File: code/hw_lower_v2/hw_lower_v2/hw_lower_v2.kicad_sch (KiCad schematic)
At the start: 22 parts, among them J1 Screw_Terminal_01x01, J2 Screw_Terminal_01x01, J3 Screw_Terminal_01x01, J4 Screw_Terminal_01x01, J5 Screw_Terminal_01x01, J6 Screw_Terminal_01x01, J7 Conn_01x06_Pin, J8 Conn_02x20_Odd_Even

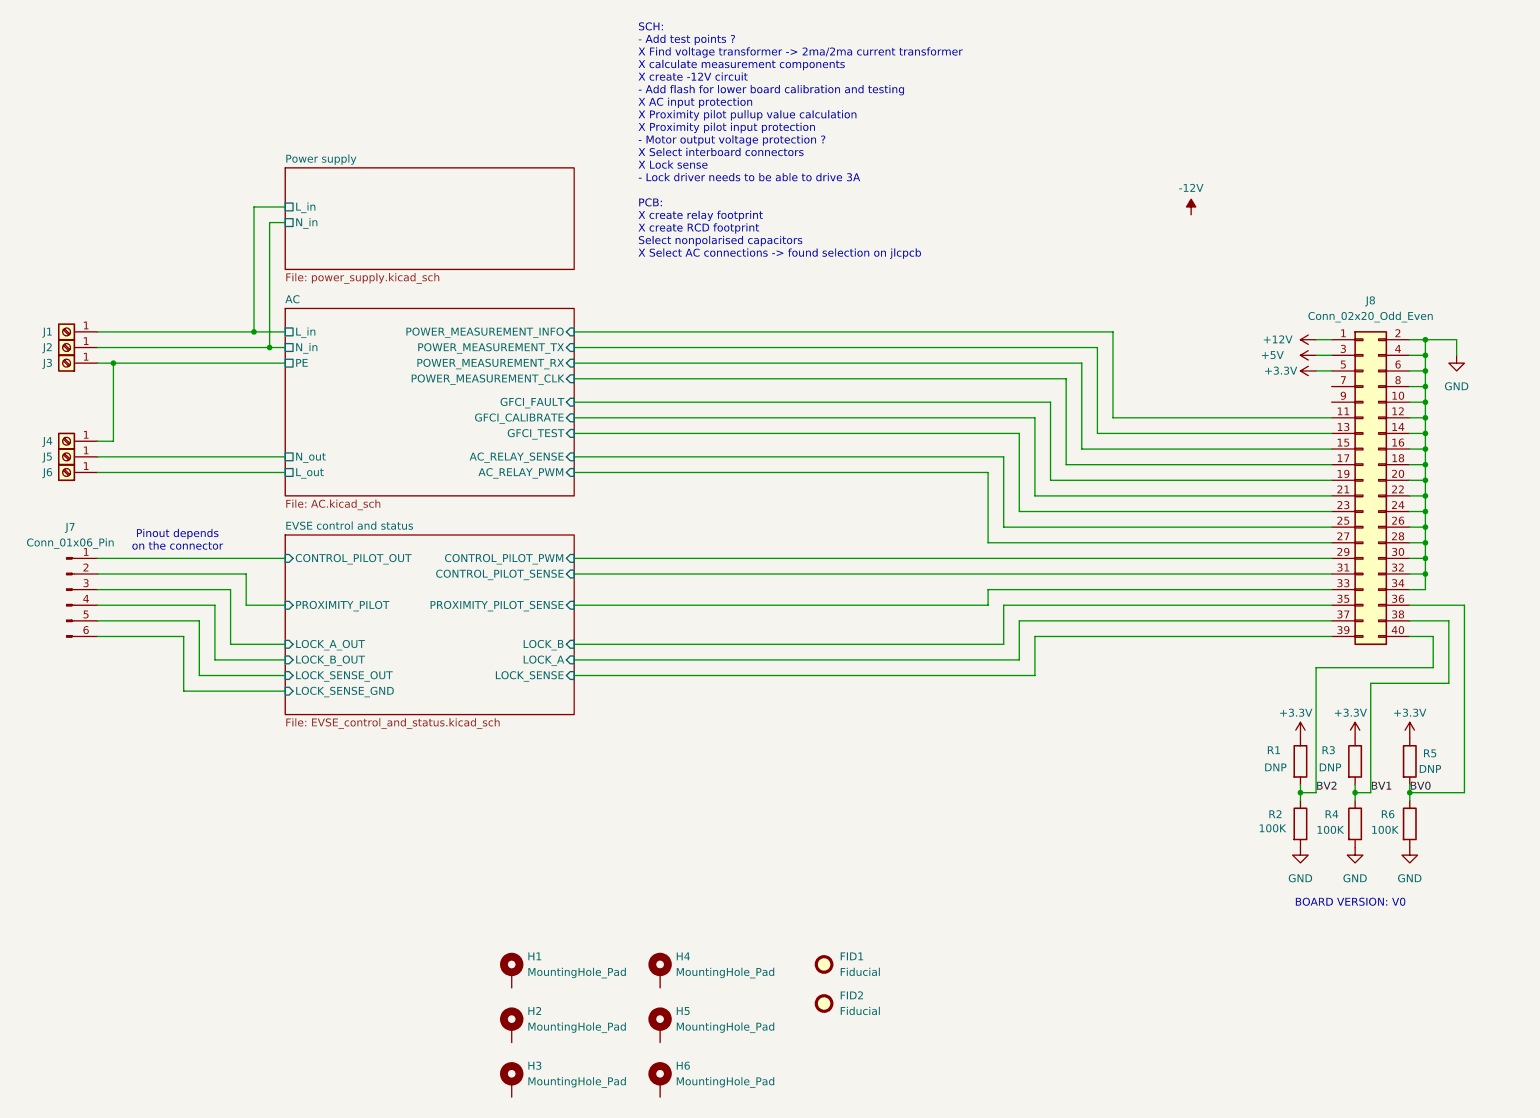
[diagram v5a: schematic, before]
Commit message: finished schematic, started first pass of layout
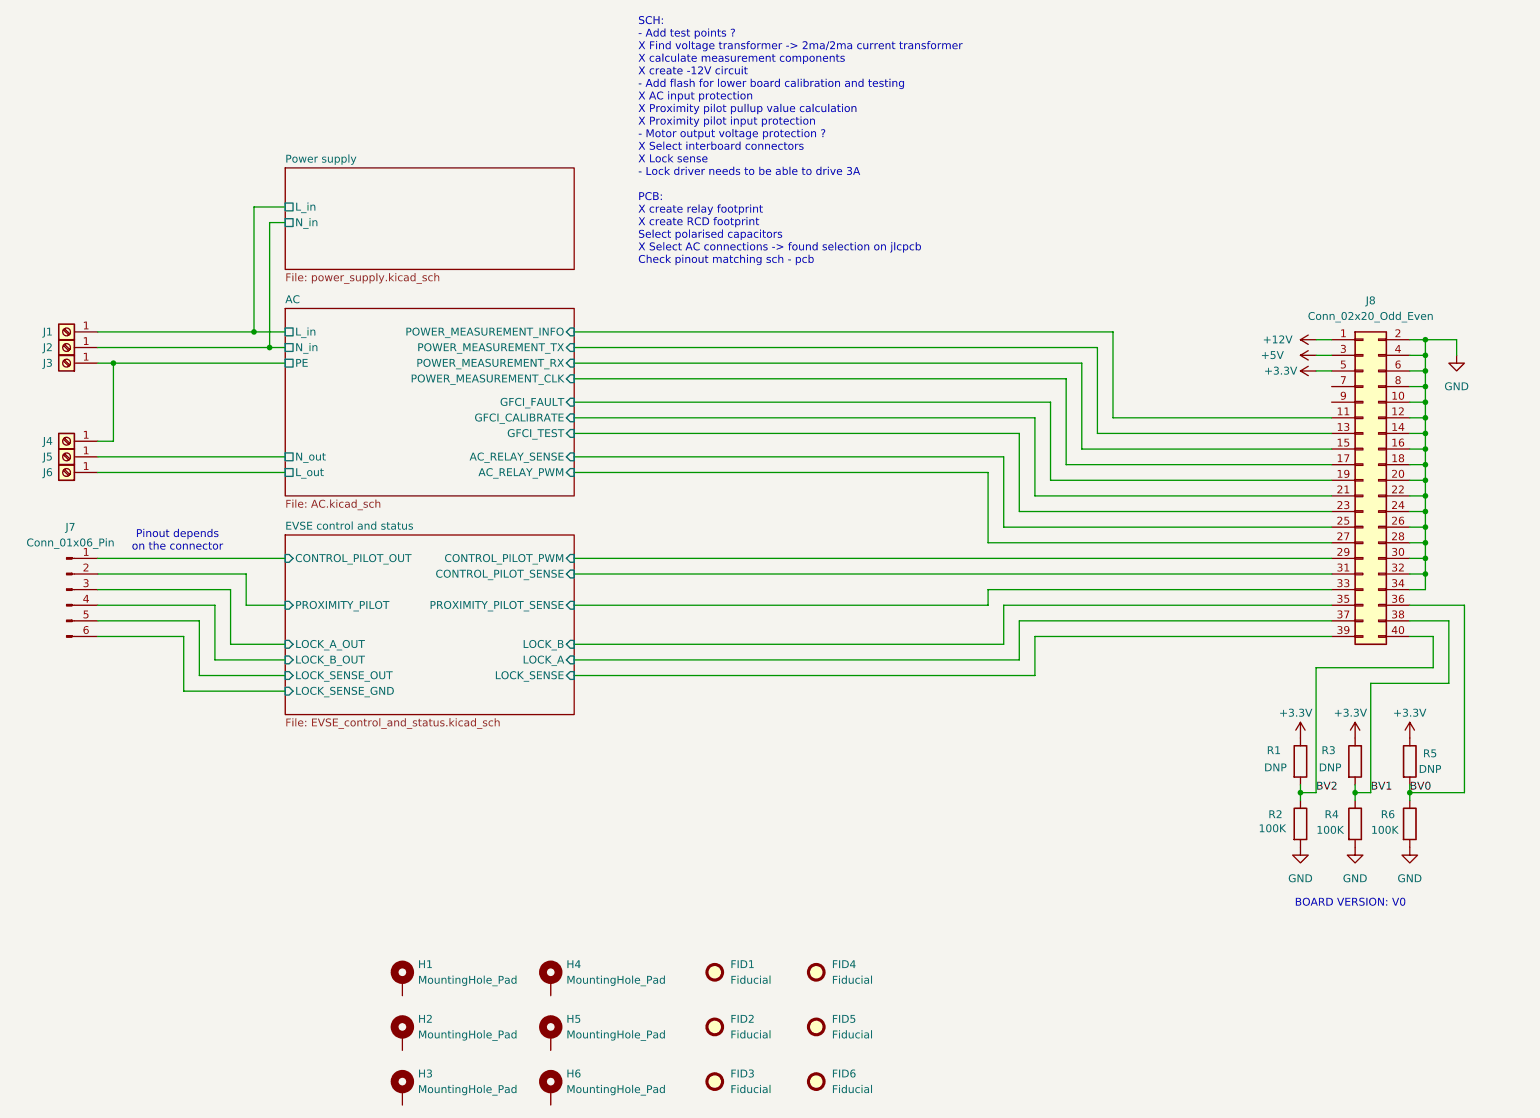
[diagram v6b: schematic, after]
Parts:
- added FID3, FID4, FID5, FID6: Fiducial, Fiducial:Fiducial_1mm_Mask3mm, symbol Mechanical:Fiducial
- FID1, FID2: footprint (none) -> Fiducial:Fiducial_1mm_Mask3mm
- H1, H2, H3, H4, H5, H6: footprint (none) -> MountingHole:MountingHole_3.2mm_M3_Pad_Via
- J1, J2, J3, J4, J5, J6: footprint (none) -> JLCPCB:CONN-TH_T44001
- J7: footprint (none) -> Connector_PinHeader_2.54mm:PinHeader_1x06_P2.54mm_Horizontal; LCSC (none) -> C56816
- J8: footprint (none) -> Connector_PinHeader_2.54mm:PinHeader_2x20_P2.54mm_Vertical
- R2, R4, R6: LCSC (none) -> C25803
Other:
- moved on the sheet: FID1, FID2, H1, H2, H3, H4, H5, H6

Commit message: further placement and pin relocation
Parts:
- H1, H2, H3, H4, H5, H6: value MountingHole_Pad -> MountingHole; footprint MountingHole:MountingHole_3.2mm_M3_Pad_Via -> MountingHole:MountingHole_3.2mm_M3_Pad; symbol Mechanical:MountingHole_Pad -> Mechanical:MountingHole
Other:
- sheet AC ports: added L_internal_power, N_internal_power; removed none
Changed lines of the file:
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@@
 	)
 	(junction
-		(at 69.85 69.85)
-		(diameter 0)
-		(color 0 0 0 0)
-	)
-	(junction
 		(at 257.81 104.14)
 		(diameter 0)
@@
 		(color 0 0 0 0)
 	)
-	(junction
-		(at 67.31 67.31)
-		(diameter 0)
-		(color 0 0 0 0)
-	)
 	(wire
 		(pts
@@
 	(wire
 		(pts
+			(xy 72.39 78.74) (xy 67.31 78.74)
+		)
+		(stroke
+			(width 0)
+			(type default)
+		)
+	)
+	(wire
+		(pts
 			(xy 119.38 118.11) (xy 189.23 118.11)
 		)
@@
 	(wire
 		(pts
-			(xy 67.31 46.99) (xy 67.31 67.31)
-		)
-		(stroke
-			(width 0)
-			(type default)
-		)
-	)
-	(wire
-		(pts
 			(xy 257.81 101.6) (xy 257.81 104.14)
 		)
@@
 	(wire
 		(pts
-			(xy 55.88 125.73) (xy 55.88 116.84)
+			(xy 69.85 49.53) (xy 69.85 81.28)
 		)
 		(stroke
@@
 	(wire
 		(pts
-			(xy 69.85 69.85) (xy 72.39 69.85)
+			(xy 55.88 125.73) (xy 55.88 116.84)
 		)
 		(stroke
@@
 	(wire
 		(pts
+			(xy 69.85 81.28) (xy 72.39 81.28)
+		)
+		(stroke
+			(width 0)
+			(type default)
+		)
+	)
+	(wire
+		(pts
 			(xy 242.57 83.82) (xy 204.47 83.82)
 		)
@@
 	(wire
 		(pts
-			(xy 67.31 67.31) (xy 72.39 67.31)
+			(xy 41.91 67.31) (xy 72.39 67.31)
 		)
 		(stroke
@@
 	(wire
 		(pts
-			(xy 41.91 69.85) (xy 69.85 69.85)
+			(xy 41.91 69.85) (xy 72.39 69.85)
 		)
 		(stroke
@@
 	(wire
 		(pts
-			(xy 257.81 88.9) (xy 257.81 91.44)
+			(xy 67.31 78.74) (xy 67.31 46.99)
 		)
 		(stroke
@@
 	(wire
 		(pts
-			(xy 255.27 86.36) (xy 257.81 86.36)
+			(xy 257.81 88.9) (xy 257.81 91.44)
 		)
 		(stroke
@@
 	(wire
 		(pts
-			(xy 69.85 49.53) (xy 69.85 69.85)
+			(xy 255.27 86.36) (xy 257.81 86.36)
 		)
 		(stroke
@@
 	(wire
 		(pts
-			(xy 41.91 67.31) (xy 67.31 67.31)
-		)
-		(stroke
-			(width 0)
-			(type default)
-		)
-	)
-	(wire
-		(pts
 			(xy 66.04 106.68) (xy 41.91 106.68)
 		)
@@
 	)
 	(symbol
-		(lib_id "Mechanical:MountingHole_Pad")
+		(lib_id "Mechanical:MountingHole")
 		(at 91.44 181.61 0)
 		(unit 1)
@@
 		(fields_autoplaced yes)
 		(property "Reference" "H2"
-			(at 93.98 179.0699 0)
+			(at 93.98 180.3399 0)
 			(effects
 				(font
@@
 			)
 		)
-		(property "Value" "MountingHole_Pad"
-			(at 93.98 181.6099 0)
+		(property "Value" "MountingHole"
+			(at 93.98 182.8799 0)
 			(effects
 				(font
@@
 			)
 		)
-		(property "Footprint" "MountingHole:MountingHole_3.2mm_M3_Pad_Via"
+		(property "Footprint" "MountingHole:MountingHole_3.2mm_M3_Pad"
 			(at 91.44 181.61 0)
 			(effects
@@
 			)
 		)
-		(property "Description" "Mounting Hole with connection"
+		(property "Description" "Mounting Hole without connection"
 			(at 91.44 181.61 0)
 			(effects
@@
 			)
 		)
-		(pin "1"
-		)
 		(instances
 			(project "hw_lower_v2"
@@
 	)
 	(symbol
-		(lib_id "Mechanical:MountingHole_Pad")
+		(lib_id "Mechanical:MountingHole")
 		(at 91.44 172.72 0)
 		(unit 1)
@@
 		(fields_autoplaced yes)
 		(property "Reference" "H1"
-			(at 93.98 170.1799 0)
+			(at 93.98 171.4499 0)
 			(effects
 				(font
@@
 			)
 		)
-		(property "Value" "MountingHole_Pad"
-			(at 93.98 172.7199 0)
+		(property "Value" "MountingHole"
+			(at 93.98 173.9899 0)
 			(effects
 				(font
@@
 			)
 		)
-		(property "Footprint" "MountingHole:MountingHole_3.2mm_M3_Pad_Via"
+		(property "Footprint" "MountingHole:MountingHole_3.2mm_M3_Pad"
 			(at 91.44 172.72 0)
 			(effects
@@
 			)
 		)
-		(property "Description" "Mounting Hole with connection"
+		(property "Description" "Mounting Hole without connection"
 			(at 91.44 172.72 0)
 			(effects
@@
 			)
 		)
-		(pin "1"
-		)
 		(instances
 			(project ""
@@
 	)
 	(symbol
-		(lib_id "Mechanical:MountingHole_Pad")
+		(lib_id "Mechanical:MountingHole")
 		(at 115.57 190.5 0)
 		(unit 1)
@@
 		(fields_autoplaced yes)
 		(property "Reference" "H6"
-			(at 118.11 187.9599 0)
+			(at 118.11 189.2299 0)
 			(effects
 				(font
@@
 			)
 		)
-		(property "Value" "MountingHole_Pad"
-			(at 118.11 190.4999 0)
+		(property "Value" "MountingHole"
+			(at 118.11 191.7699 0)
 			(effects
 				(font
@@
 			)
 		)
-		(property "Footprint" "MountingHole:MountingHole_3.2mm_M3_Pad_Via"
+		(property "Footprint" "MountingHole:MountingHole_3.2mm_M3_Pad"
 			(at 115.57 190.5 0)
 			(effects
@@
 			)
 		)
-		(property "Description" "Mounting Hole with connection"
+		(property "Description" "Mounting Hole without connection"
 			(at 115.57 190.5 0)
 			(effects
@@
 			)
 		)
-		(pin "1"
-		)
 		(instances
 			(project "hw_lower_v2"
@@
 	)
 	(symbol
-		(lib_id "Mechanical:MountingHole_Pad")
+		(lib_id "Mechanical:MountingHole")
 		(at 115.57 172.72 0)
 		(unit 1)
@@
 		(fields_autoplaced yes)
 		(property "Reference" "H4"
-			(at 118.11 170.1799 0)
+			(at 118.11 171.4499 0)
 			(effects
 				(font
@@
 			)
 		)
-		(property "Value" "MountingHole_Pad"
-			(at 118.11 172.7199 0)
+		(property "Value" "MountingHole"
+			(at 118.11 173.9899 0)
 			(effects
 				(font
@@
 			)
 		)
-		(property "Footprint" "MountingHole:MountingHole_3.2mm_M3_Pad_Via"
+		(property "Footprint" "MountingHole:MountingHole_3.2mm_M3_Pad"
 			(at 115.57 172.72 0)
 			(effects
@@
 			)
 		)
-		(property "Description" "Mounting Hole with connection"
+		(property "Description" "Mounting Hole without connection"
 			(at 115.57 172.72 0)
 			(effects
@@
 			)
 		)
-		(pin "1"
-		)
 		(instances
 			(project "hw_lower_v2"
@@
 	)
 	(symbol
-		(lib_id "Mechanical:MountingHole_Pad")
+		(lib_id "Mechanical:MountingHole")
 		(at 115.57 181.61 0)
 		(unit 1)
@@
 		(fields_autoplaced yes)
 		(property "Reference" "H5"
-			(at 118.11 179.0699 0)
+			(at 118.11 180.3399 0)
 			(effects
 				(font
@@
 			)
 		)
-		(property "Value" "MountingHole_Pad"
-			(at 118.11 181.6099 0)
+		(property "Value" "MountingHole"
+			(at 118.11 182.8799 0)
 			(effects
 				(font
@@
 			)
 		)
-		(property "Footprint" "MountingHole:MountingHole_3.2mm_M3_Pad_Via"
+		(property "Footprint" "MountingHole:MountingHole_3.2mm_M3_Pad"
 			(at 115.57 181.61 0)
 			(effects
@@
 			)
 		)
-		(property "Description" "Mounting Hole with connection"
+		(property "Description" "Mounting Hole without connection"
 			(at 115.57 181.61 0)
 			(effects
@@
 			)
 		)
-		(pin "1"
-		)
 		(instances
 			(project "hw_lower_v2"
@@
 	)
 	(symbol
-		(lib_id "Mechanical:MountingHole_Pad")
+		(lib_id "Mechanical:MountingHole")
 		(at 91.44 190.5 0)
 		(unit 1)
@@
 		(fields_autoplaced yes)
 		(property "Reference" "H3"
-			(at 93.98 187.9599 0)
+			(at 93.98 189.2299 0)
 			(effects
 				(font
@@
 			)
 		)
-		(property "Value" "MountingHole_Pad"
-			(at 93.98 190.4999 0)
+		(property "Value" "MountingHole"
+			(at 93.98 191.7699 0)
 			(effects
 				(font
@@
 			)
 		)
-		(property "Footprint" "MountingHole:MountingHole_3.2mm_M3_Pad_Via"
+		(property "Footprint" "MountingHole:MountingHole_3.2mm_M3_Pad"
 			(at 91.44 190.5 0)
 			(effects
@@
 			)
 		)
-		(property "Description" "Mounting Hole with connection"
+		(property "Description" "Mounting Hole without connection"
 			(at 91.44 190.5 0)
 			(effects
@@
 			)
 		)
-		(pin "1"
-		)
 		(instances
 			(project "hw_lower_v2"
@@
 			)
 		)
+		(pin "N_internal_power" bidirectional
+			(at 72.39 81.28 180)
+			(effects
+				(font
+					(size 1.27 1.27)
+				)
+				(justify left)
+			)
+		)
+		(pin "L_internal_power" bidirectional
+			(at 72.39 78.74 180)
+			(effects
+				(font
+					(size 1.27 1.27)
+				)
+				(justify left)
+			)
+		)

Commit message: commit before experimenting
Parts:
- H1, H2: footprint MountingHole:MountingHole_3.2mm_M3_Pad -> MountingHole:MountingHole_3.2mm_M3
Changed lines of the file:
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@@
 			)
 		)
-		(property "Footprint" "MountingHole:MountingHole_3.2mm_M3_Pad"
+		(property "Footprint" "MountingHole:MountingHole_3.2mm_M3"
 			(at 91.44 181.61 0)
 			(effects
@@
 			)
 		)
-		(property "Footprint" "MountingHole:MountingHole_3.2mm_M3_Pad"
+		(property "Footprint" "MountingHole:MountingHole_3.2mm_M3"
 			(at 91.44 172.72 0)
 			(effects
